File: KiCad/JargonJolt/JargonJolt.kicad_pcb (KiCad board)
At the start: 2 copper layers, 1 part, among them U1 ESP32-S3-WROOM-1-N16R2

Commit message: began working on schematic
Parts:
- added C1: C, Capacitor_SMD:C_0805_2012Metric, F.Cu at (135.2, 80.1)
- added C2: C, Capacitor_SMD:C_0805_2012Metric, F.Cu at (135.2, 83.1)
- added C3: C, Capacitor_SMD:C_0805_2012Metric, F.Cu at (135.2, 86.1)
- added C4: C, Capacitor_SMD:C_0805_2012Metric, F.Cu at (135.2, 89.1)
- added Q1: SS8050-G, Package_TO_SOT_SMD:SOT-23, F.Cu at (135.5, 92.8)
- added Q2: SS8050-G, Package_TO_SOT_SMD:SOT-23, F.Cu at (135.5, 97.3)
- added R1: R, Resistor_SMD:R_0805_2012Metric, F.Cu at (130.8, 80.0)
- added R2: R, Resistor_SMD:R_0805_2012Metric, F.Cu at (130.8, 83.0)
- added R3: 1k, Resistor_SMD:R_0805_2012Metric, F.Cu at (130.8, 85.9)
- added R4: R, Resistor_SMD:R_0805_2012Metric, F.Cu at (130.8, 88.9)
- added R5: R, Resistor_SMD:R_0805_2012Metric, F.Cu at (130.8, 91.8)
- added R6: R, Resistor_SMD:R_0805_2012Metric, F.Cu at (130.8, 94.8)
- added R7: R, Resistor_SMD:R_0805_2012Metric, F.Cu at (130.8, 97.7)
- added R8: R, Resistor_SMD:R_0805_2012Metric, F.Cu at (130.8, 100.7)
- U1: footprint ESP32-S3-WROOM:XCVR_ESP32-S3-WROOM-1-N16R2 -> Espressif:ESP32-S3-WROOM-1
- moved U1 28.4 mm to (160.9, 103.3)
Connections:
- U1 pad 1: unconnected-(U1-GND-Pad1) -> GND
- U1 pad 15: unconnected-(U1-IO3-Pad15) -> /MCU/GPIO3_STRAP
- U1 pad 16: unconnected-(U1-IO46-Pad16) -> /MCU/GPIO46_STRAP
- U1 pad 2: unconnected-(U1-3V3-Pad2) -> +3V3
- U1 pad 26: unconnected-(U1-IO45-Pad26) -> /MCU/GPIO45_STRAP
- U1 pad 27: unconnected-(U1-IO0-Pad27) -> /MCU/GPIO0_STRAP
- U1 pad 3: unconnected-(U1-EN-Pad3) -> /MCU/CHIP_PU
- U1 pad 36: unconnected-(U1-RXD0-Pad36) -> /MCU/Tx
- U1 pad 37: unconnected-(U1-TXD0-Pad37) -> /MCU/Rx
- U1 pad 40: unconnected-(U1-GND-Pad40) -> GND

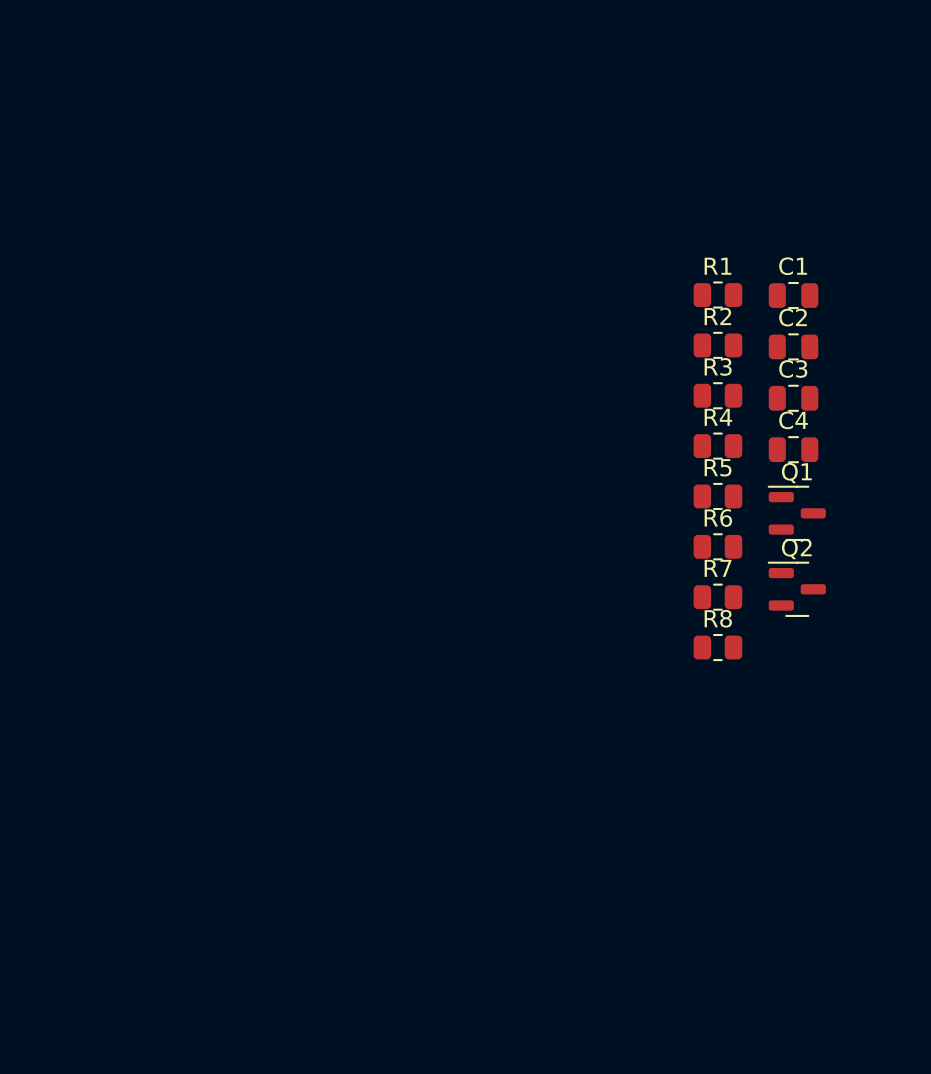
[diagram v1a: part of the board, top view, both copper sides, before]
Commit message: added more footprints
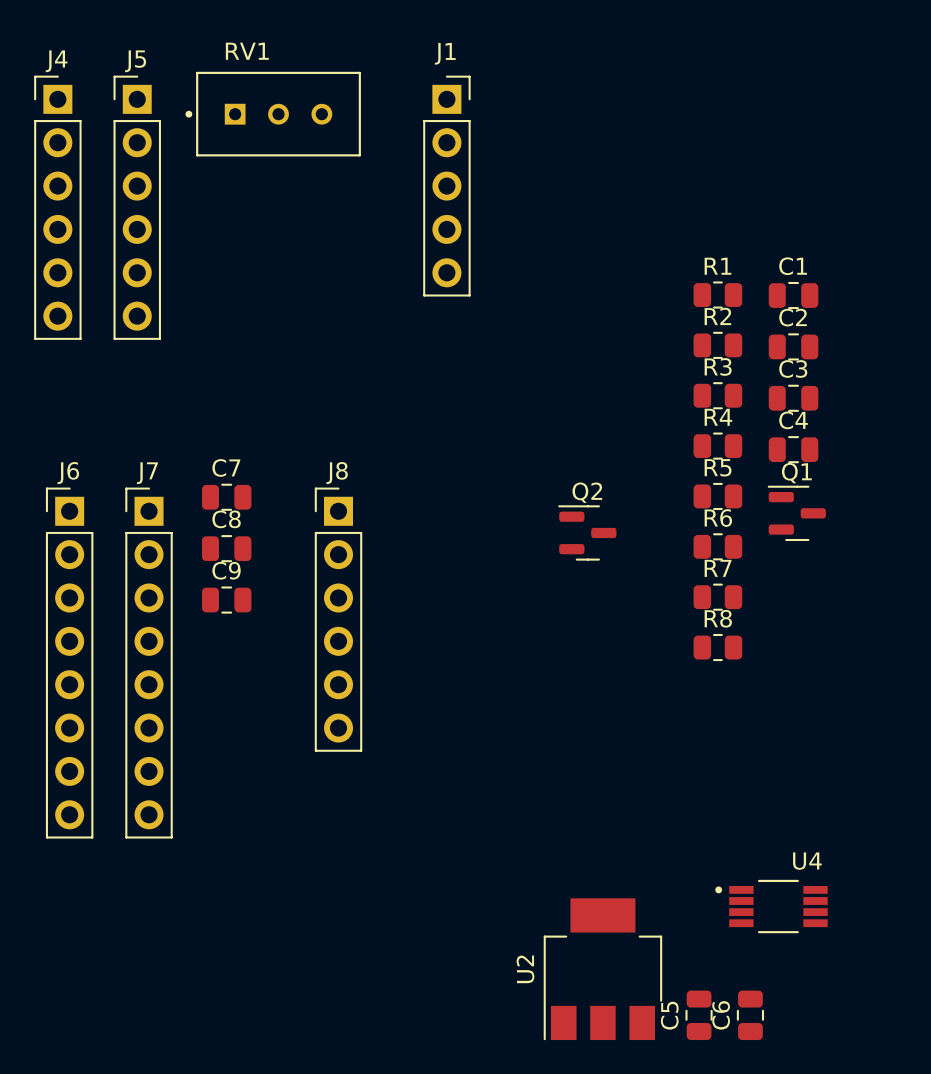
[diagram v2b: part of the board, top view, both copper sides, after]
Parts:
- added C5: C, Capacitor_SMD:C_0805_2012Metric, F.Cu at (129.7, 122.2)
- added C6: C, Capacitor_SMD:C_0805_2012Metric, F.Cu at (132.7, 122.2)
- added C7: 0.1uF, Capacitor_SMD:C_0805_2012Metric, F.Cu at (102.0, 91.9)
- added C8: 0.1uF, Capacitor_SMD:C_0805_2012Metric, F.Cu at (102.0, 94.9)
- added C9: 0.1uF, Capacitor_SMD:C_0805_2012Metric, F.Cu at (102.0, 97.9)
- added J1: Conn_01x05, Connector_PinSocket_2.54mm:PinSocket_1x05_P2.54mm_Vertical, F.Cu at (114.9, 68.6)
- added J4: Conn_01x06, Connector_PinHeader_2.54mm:PinHeader_1x06_P2.54mm_Vertical, F.Cu at (92.1, 68.6)
- added J5: Conn_01x06, Connector_PinHeader_2.54mm:PinHeader_1x06_P2.54mm_Vertical, F.Cu at (96.8, 68.6)
- added J6: Conn_01x08, Connector_PinHeader_2.54mm:PinHeader_1x08_P2.54mm_Vertical, F.Cu at (92.8, 92.7)
- added J7: Conn_01x08, Connector_PinHeader_2.54mm:PinHeader_1x08_P2.54mm_Vertical, F.Cu at (97.5, 92.7)
- added J8: Conn_01x06, Connector_PinHeader_2.54mm:PinHeader_1x06_P2.54mm_Vertical, F.Cu at (108.6, 92.7)
- added RV1: 100k_Potentiometer, Espressif:TRIM_3296W-1-104LF, F.Cu at (105.1, 69.5)
- added U2: ADP3339, Package_TO_SOT_SMD:SOT-223-3_TabPin2, F.Cu at (124.1, 119.5)
- added U4: 74LVC3G17DP_125, Espressif:SOP65P490X110-8N, F.Cu at (134.4, 115.9)
- R3: value 1k -> R
- R6: value R -> 1k
- moved Q2 12.7 mm to (123.2, 94.0)
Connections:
- C1 pad 1: +3V3 -> /MCU/CHIP_PU
- C2 pad 1: +3V3 -> /MCU/GPIO0_STRAP
- C3 pad 1: /MCU/CHIP_PU -> +3.3VA
- C4 pad 1: /MCU/GPIO0_STRAP -> +3.3VA
- R1 pad 1: +3V3 -> +3.3VA
- R2 pad 1: Net-(JP1-C) -> +3.3VA
- R2 pad 2: /MCU/GPIO3_STRAP -> /MCU/GPIO0_STRAP
- R3 pad 1: +3V3 -> Net-(Q1-B)
- R3 pad 2: /MCU/GPIO46_STRAP -> /MCU/DTR
- R4 pad 1: +3V3 -> Net-(Q2-B)
- R4 pad 2: /MCU/GPIO0_STRAP -> /MCU/RTS
- R5 pad 1: /MCU/CHIP_PU -> Net-(JP1-C)
- R5 pad 2: Net-(Q1-C) -> /MCU/GPIO3_STRAP
- R6 pad 1: Net-(Q1-B) -> +3.3VA
- R6 pad 2: /MCU/DTR -> /MCU/GPIO46_STRAP
- R7 pad 1: /MCU/GPIO0_STRAP -> /MCU/CHIP_PU
- R7 pad 2: Net-(Q2-C) -> Net-(Q1-C)
- R8 pad 1: Net-(Q2-B) -> /MCU/GPIO0_STRAP
- R8 pad 2: /MCU/RTS -> Net-(Q2-C)
- U1 pad 10: unconnected-(U1-IO17-Pad10) -> /MCU/I2S_LRCLK
- U1 pad 11: unconnected-(U1-IO18-Pad11) -> /MCU/I2S_BCLK
- U1 pad 13: unconnected-(U1-IO19-Pad13) -> /MCU/I2S_DATA
- U1 pad 18: unconnected-(U1-IO10-Pad18) -> /MCU/HSPI_SCLK
- U1 pad 19: unconnected-(U1-IO11-Pad19) -> /MCU/HSPI_MISO
- U1 pad 2: +3V3 -> +3.3VA
- U1 pad 20: unconnected-(U1-IO12-Pad20) -> /MCU/HSPI_MOSI
- U1 pad 23: unconnected-(U1-IO21-Pad23) -> /MCU/WS
- U1 pad 28: unconnected-(U1-IO35-Pad28) -> /MCU/DIN/DOUT
- U1 pad 29: unconnected-(U1-IO36-Pad29) -> /MCU/RST
- U1 pad 30: unconnected-(U1-IO37-Pad30) -> /MCU/CS0
- U1 pad 31: unconnected-(U1-IO38-Pad31) -> /MCU/CS1
- U1 pad 32: unconnected-(U1-IO39-Pad32) -> /MCU/CS2
- U1 pad 33: unconnected-(U1-IO40-Pad33) -> /MCU/VSPI_SCLK
- U1 pad 34: unconnected-(U1-IO41-Pad34) -> /MCU/VSPI_MISO
- U1 pad 35: unconnected-(U1-IO42-Pad35) -> /MCU/VSPI_MOSI
- U1 pad 4: unconnected-(U1-IO4-Pad4) -> /MCU/BUTTON1
- U1 pad 5: unconnected-(U1-IO5-Pad5) -> /MCU/BUTTON2
- U1 pad 6: unconnected-(U1-IO6-Pad6) -> /MCU/BUTTON3
- U1 pad 7: unconnected-(U1-IO7-Pad7) -> /MCU/BUSY

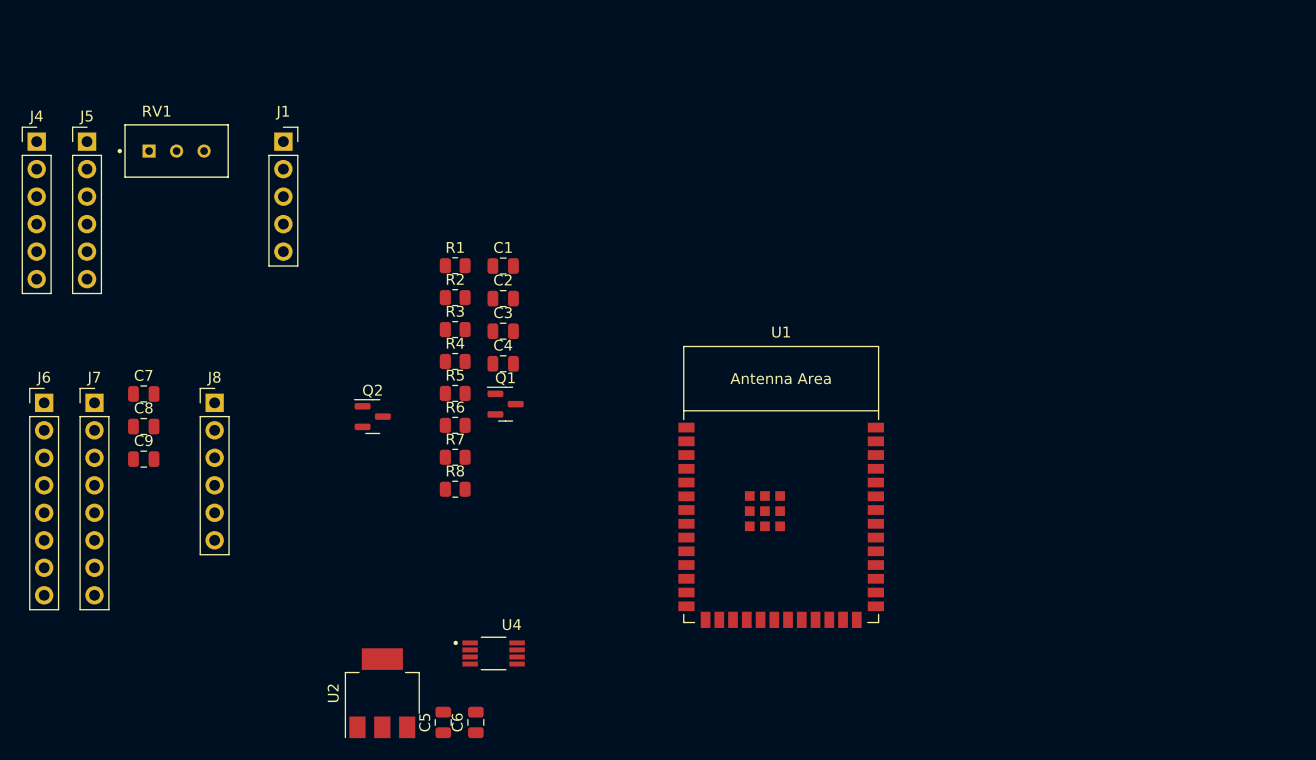
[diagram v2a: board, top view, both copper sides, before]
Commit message: added more footprints
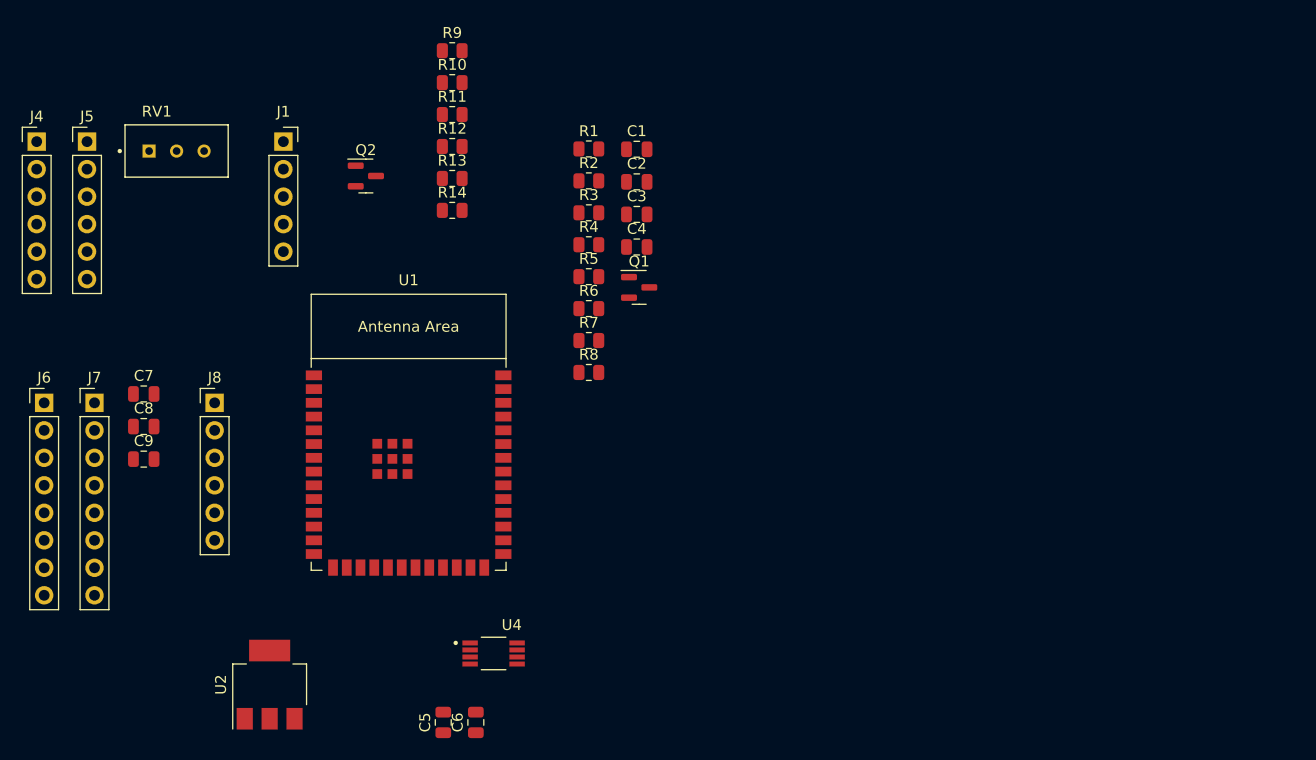
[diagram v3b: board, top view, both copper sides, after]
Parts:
- added R10: 1k, Resistor_SMD:R_0805_2012Metric, F.Cu at (130.5, 63.1)
- added R11: 1M, Resistor_SMD:R_0805_2012Metric, F.Cu at (130.5, 66.1)
- added R12: 1k, Resistor_SMD:R_0805_2012Metric, F.Cu at (130.5, 69.0)
- added R13: 1M, Resistor_SMD:R_0805_2012Metric, F.Cu at (130.5, 72.0)
- added R14: 1k, Resistor_SMD:R_0805_2012Metric, F.Cu at (130.5, 74.9)
- added R9: 1M, Resistor_SMD:R_0805_2012Metric, F.Cu at (130.5, 60.2)
- moved U1 34.8 mm to (126.5, 98.4)
- moved Q2 22.2 mm to (122.6, 71.8)
- moved C1 16.4 mm to (147.6, 69.3)
- moved C4 16.4 mm to (147.6, 78.3)
- moved R1 16.4 mm to (143.2, 69.3)
- moved R2 16.4 mm to (143.2, 72.2)
- moved R6 16.4 mm to (143.2, 84.0)
- moved R7 16.4 mm to (143.2, 87.0)
- moved C2 16.4 mm to (147.6, 72.3)
- moved C3 16.4 mm to (147.6, 75.3)
- moved Q1 16.4 mm to (147.8, 82.0)
- moved R3 16.4 mm to (143.2, 75.2)
- moved R4 16.4 mm to (143.2, 78.1)
- moved R5 16.4 mm to (143.2, 81.1)
- moved R8 16.4 mm to (143.2, 89.9)
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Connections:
- U4 pad 8: unconnected-(U4-VCC-Pad8) -> +3.3VA

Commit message: PCB first revision
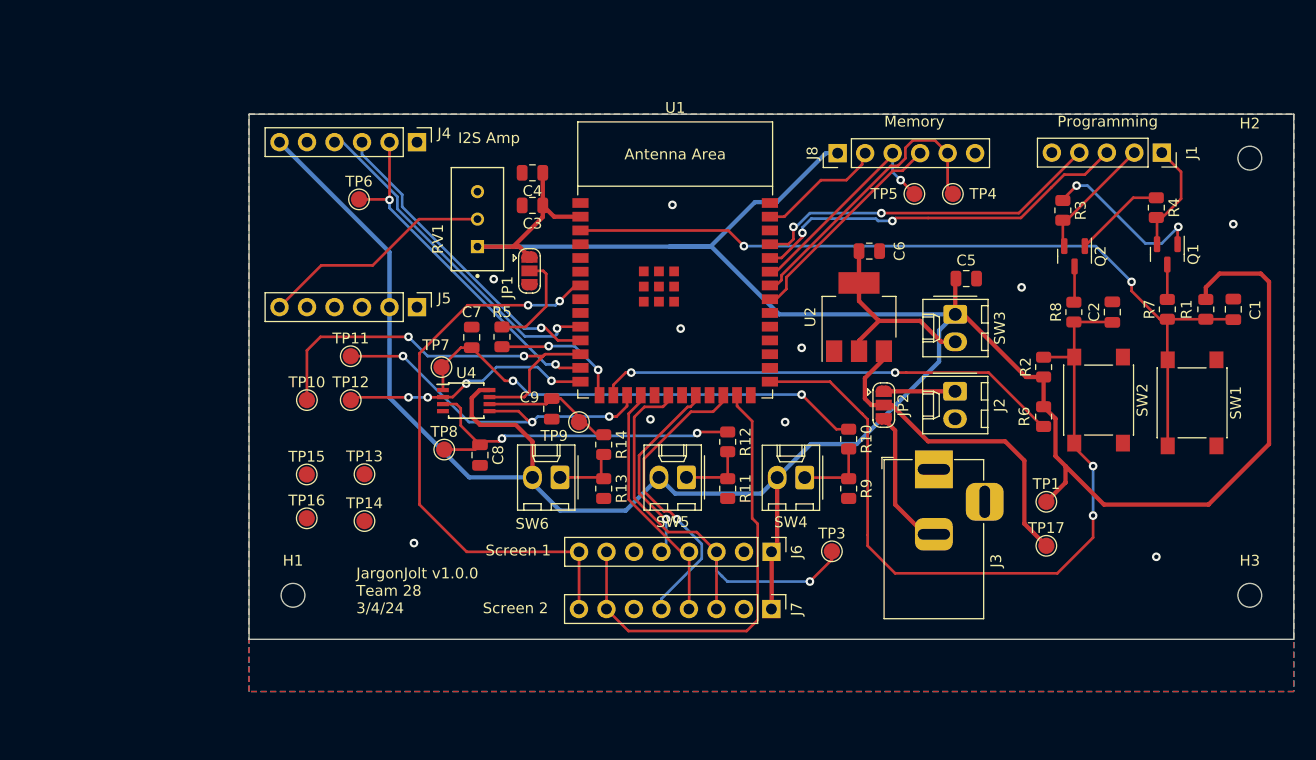
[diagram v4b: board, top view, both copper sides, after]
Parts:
- added H1: MountingHole, MountingHole:MountingHole_2.2mm_M2, F.Cu at (115.8, 110.5)
- added H2: MountingHole, MountingHole:MountingHole_2.2mm_M2, F.Cu at (204.2, 70.1)
- added H3: MountingHole, MountingHole:MountingHole_2.2mm_M2, F.Cu at (204.2, 110.5)
- added J2: Conn_01x02, Connector_Molex:Molex_KK-254_AE-6410-02A_1x02_P2.54mm_Vertical, F.Cu at (177.0, 91.6)
- added J3: Conn_01x02, Connector_BarrelJack:BarrelJack_Horizontal, F.Cu at (175.0, 98.9)
- added JP1: SolderJumper_3_Open, Jumper:SolderJumper-3_P1.3mm_Open_RoundedPad1.0x1.5mm, F.Cu at (137.7, 80.5)
- added JP2: SolderJumper_3_Open, Jumper:SolderJumper-3_P1.3mm_Open_RoundedPad1.0x1.5mm, F.Cu at (170.4, 92.9)
- added SW1: SW_Push, Button_Switch_SMD:SW_Push_1P1T_NO_6x6mm_H9.5mm, F.Cu at (198.9, 92.7)
- added SW2: SW_Push, Button_Switch_SMD:SW_Push_1P1T_NO_6x6mm_H9.5mm, F.Cu at (190.2, 92.5)
- added SW3: SW_DIP_x01, Connector_Molex:Molex_KK-254_AE-6410-02A_1x02_P2.54mm_Vertical, F.Cu at (177.0, 84.5)
- added SW4: SW_Push, Connector_Molex:Molex_KK-254_AE-6410-02A_1x02_P2.54mm_Vertical, F.Cu at (163.1, 99.6)
- added SW5: SW_Push, Connector_Molex:Molex_KK-254_AE-6410-02A_1x02_P2.54mm_Vertical, F.Cu at (152.2, 99.6)
- added SW6: SW_Push, Connector_Molex:Molex_KK-254_AE-6410-02A_1x02_P2.54mm_Vertical, F.Cu at (140.5, 99.6)
- added TP1: TestPoint, TestPoint:TestPoint_Pad_D1.5mm, F.Cu at (185.4, 101.9)
- added TP10: TestPoint, TestPoint:TestPoint_Pad_D1.5mm, F.Cu at (117.1, 92.5)
- added TP11: TestPoint, TestPoint:TestPoint_Pad_D1.5mm, F.Cu at (121.2, 88.4)
- added TP12: TestPoint, TestPoint:TestPoint_Pad_D1.5mm, F.Cu at (121.2, 92.5)
- added TP13: TestPoint, TestPoint:TestPoint_Pad_D1.5mm, F.Cu at (122.4, 99.3)
- added TP14: TestPoint, TestPoint:TestPoint_Pad_D1.5mm, F.Cu at (122.4, 103.6)
- added TP15: TestPoint, TestPoint:TestPoint_Pad_D1.5mm, F.Cu at (117.1, 99.3)
- added TP16: TestPoint, TestPoint:TestPoint_Pad_D1.5mm, F.Cu at (117.1, 103.4)
- added TP17: TestPoint, TestPoint:TestPoint_Pad_D1.5mm, F.Cu at (185.4, 105.9)
- added TP3: TestPoint, TestPoint:TestPoint_Pad_D1.5mm, F.Cu at (165.6, 106.4)
- added TP4: TestPoint, TestPoint:TestPoint_Pad_D1.5mm, F.Cu at (176.8, 73.4)
- added TP5: TestPoint, TestPoint:TestPoint_Pad_D1.5mm, F.Cu at (173.2, 73.4)
- added TP6: TestPoint, TestPoint:TestPoint_Pad_D1.5mm, F.Cu at (121.9, 73.9)
- added TP7: TestPoint, TestPoint:TestPoint_Pad_D1.5mm, F.Cu at (129.5, 89.4)
- added TP8: TestPoint, TestPoint:TestPoint_Pad_D1.5mm, F.Cu at (129.8, 97.0)
- added TP9: TestPoint, TestPoint:TestPoint_Pad_D1.5mm, F.Cu at (142.2, 94.5)
- U4: footprint Espressif:SOP65P490X110-8N -> Package_SO:TSSOP-8_3x3mm_P0.65mm
- moved J1 81.2 mm to (196.1, 69.6), turned to -90 degrees
- moved J6 68.6 mm to (160.0, 106.5), turned to -90 degrees
- moved Q2 65.9 mm to (188.0, 79.2), turned to -90 degrees
- moved J7 65.4 mm to (160.0, 111.8), turned to -90 degrees
- moved U2 64.2 mm to (168.1, 84.8)
- moved C5 63.4 mm to (178.0, 81.2), turned to 0 degrees
- moved J8 62.0 mm to (166.1, 69.6), turned to 90 degrees
- moved R1 58.9 mm to (200.2, 84.1), turned to -90 degrees
- moved C1 57.1 mm to (202.7, 84.1), turned to 90 degrees
- moved C6 56.7 mm to (169.1, 78.7), turned to 0 degrees
- moved R9 54.6 mm to (167.2, 100.6), turned to -90 degrees
- moved R7 53.5 mm to (196.6, 84.1), turned to 90 degrees
- moved R4 52.5 mm to (195.6, 74.7), turned to -90 degrees
- moved R10 49.3 mm to (167.2, 96.1), turned to -90 degrees
- moved Q1 48.9 mm to (196.6, 79.0), turned to -90 degrees
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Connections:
- J5 pad 1: Net-(J5-Pin_1) -> /User Interface/SPK-
- J5 pad 2: /User Interface/SD -> +3.3VA
- J5 pad 3: /User Interface/NC -> GND
- J5 pad 4: GND -> /User Interface/NC
- J5 pad 5: +3.3VA -> /User Interface/SD
- J5 pad 6: /User Interface/SPK- -> Net-(J5-Pin_6)
- RV1 pad 2: Net-(J5-Pin_1) -> Net-(J5-Pin_6)
- U1 pad 12: unconnected-(U1-IO8-Pad12) -> /MCU/BUTTON1
- U1 pad 14: unconnected-(U1-IO20-Pad14) -> /MCU/BUTTON3
- U1 pad 17: unconnected-(U1-IO9-Pad17) -> /MCU/BUTTON2
- U1 pad 22: unconnected-(U1-IO14-Pad22) -> /MCU/CS1
- U1 pad 24: unconnected-(U1-IO47-Pad24) -> /MCU/CS2
- U1 pad 25: unconnected-(U1-IO48-Pad25) -> /MCU/RST
- U1 pad 29: /MCU/RST -> unconnected-(U1-IO36-Pad29)
- U1 pad 30: /MCU/CS0 -> unconnected-(U1-IO37-Pad30)
- U1 pad 31: /MCU/CS1 -> unconnected-(U1-IO38-Pad31)
- U1 pad 32: /MCU/CS2 -> unconnected-(U1-IO39-Pad32)
- U1 pad 39: unconnected-(U1-IO1-Pad39) -> /MCU/CS0
- U1 pad 4: /MCU/BUTTON1 -> unconnected-(U1-IO4-Pad4)
- U1 pad 5: /MCU/BUTTON2 -> unconnected-(U1-IO5-Pad5)
- U1 pad 6: /MCU/BUTTON3 -> unconnected-(U1-IO6-Pad6)
- U2 pad 3: Net-(JP2-C) -> /Power/P_in
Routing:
- net +3.3VA: track 0.00 -> 277.1 mm
- net /MCU/CHIP_PU: track 0.00 -> 75.9 mm, vias 0 -> 2
- net /MCU/GPIO0_STRAP: track 0.00 -> 72.5 mm, vias 0 -> 2
- net /MCU/BUSY: track 0.00 -> 53.6 mm, vias 0 -> 2
- net Net-(U4-1A): track 0.00 -> 43.5 mm, vias 0 -> 2
- net /MCU/GPIO46_STRAP: track 0.00 -> 43.2 mm, vias 0 -> 2
- net /MCU/RST: track 0.00 -> 42.6 mm
- net /MCU/HSPI_MOSI: track 0.00 -> 41.2 mm, vias 0 -> 1
- net /MCU/BUTTON1: track 0.00 -> 39.2 mm, vias 0 -> 2
- net /MCU/Tx: track 0.00 -> 35.9 mm, vias 0 -> 2
- net /MCU/BUTTON2: track 0.00 -> 34.0 mm, vias 0 -> 3
- net Net-(U4-2A): track 0.00 -> 32.8 mm, vias 0 -> 2
- net /MCU/Rx: track 0.00 -> 32.8 mm, vias 0 -> 2
- net /MCU/I2S_DATA: track 0.00 -> 32.7 mm, vias 0 -> 2
- net /MCU/I2S_LRCLK: track 0.00 -> 31.5 mm, vias 0 -> 1
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- added copper zone on B.Cu, net GND
- added copper zone on F.Cu, net GND
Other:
- board outline added: 96.5 x 48.5 mm
- board text added: "I2S Amp"
- board text added: "JargonJolt v1.0.0 Team 28 3/4/24"
- board text added: "Memory"
- board text added: "Programming"
- board text added: "Screen 1"
- board text added: "Screen 2"
